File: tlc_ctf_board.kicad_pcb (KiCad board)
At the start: 2 copper layers, 78 x 51 mm, 15 parts, among them J1 AVR-ISP-6, U1 ATtiny84A-SSU

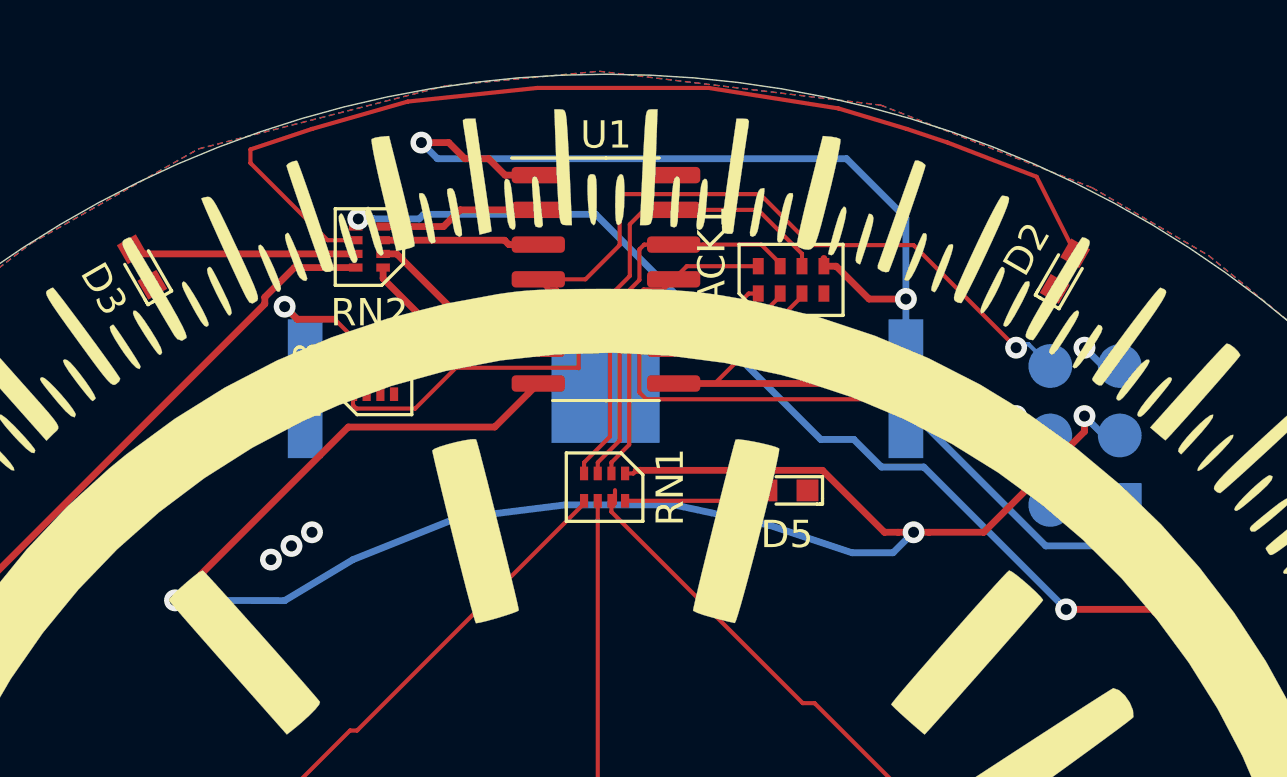
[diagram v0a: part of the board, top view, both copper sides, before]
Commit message: fix connections per qtouch, reroute.  switch to discrete caps
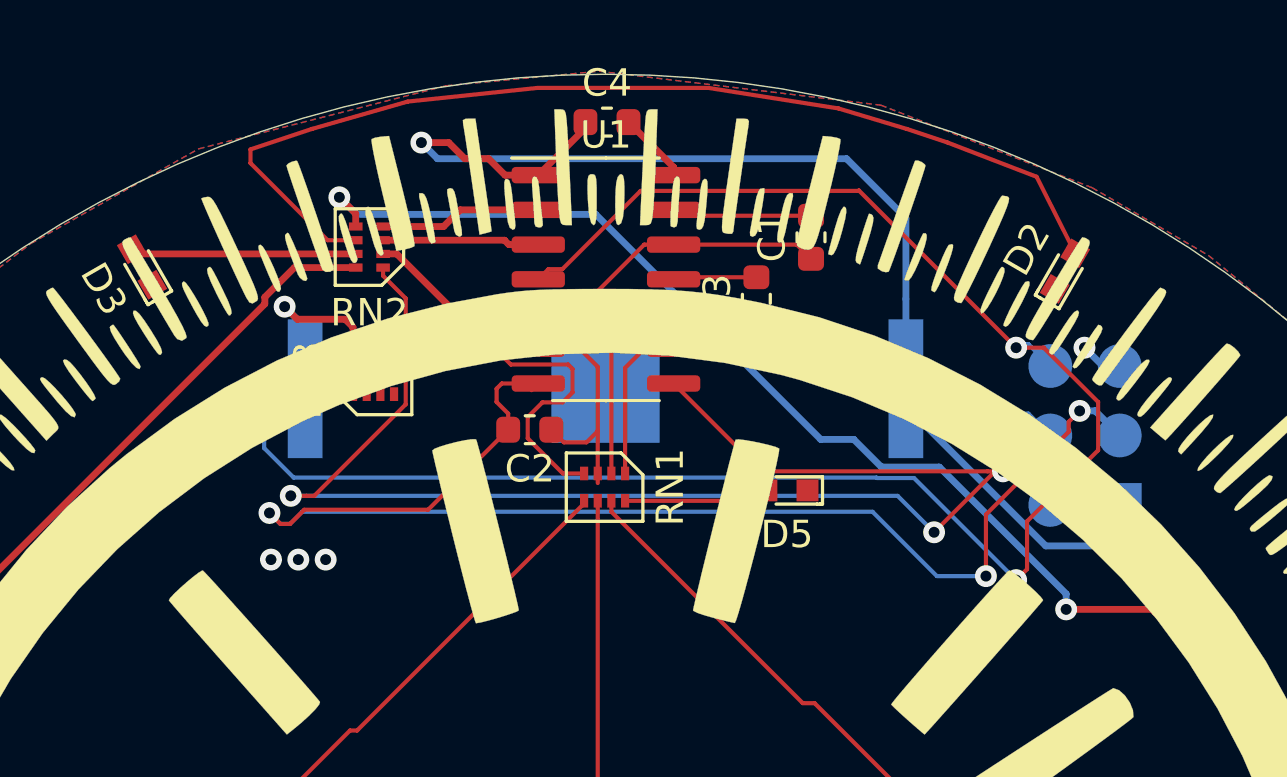
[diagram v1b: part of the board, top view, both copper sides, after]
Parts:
- removed CPACK1: C_Pack_4, tlc_ctf_board:CAP_ARRAY_4_1206
- removed the G*** at (174.0, 67.0) (x2)
- added C1: C, Capacitor_SMD:C_0603_1608Metric, F.Cu at (181.5, 47.4)
- added C2: C, Capacitor_SMD:C_0603_1608Metric, F.Cu at (171.2, 54.5)
- added C3: C, Capacitor_SMD:C_0603_1608Metric, F.Cu at (179.5, 49.7)
- added C4: C, Capacitor_SMD:C_0603_1608Metric, F.Cu at (174.0, 43.2)
- added G***: LOGO, tlc_ctf_board:logo, B.Cu at (174.0, 67.0)
- added G***: LOGO, tlc_ctf_board:logo, F.Cu at (174.0, 67.0)
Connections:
- J1 pad 1: MISO -> LED2
- J1 pad 3: QT5 -> LED1
- J1 pad 4: LED1 -> MOSI
- RN1 pad 2: QT2 -> SNSK1
- RN1 pad 3: QT3 -> SNSK2
- RN1 pad 4: QT1 -> SNSK0
- U1 pad 10: QT4 -> SNSK1
- U1 pad 11: QT2 -> SNS1
- U1 pad 12: QT3 -> SNSK0
- U1 pad 13: QT1 -> SNS0
- U1 pad 6: LED2 -> SNSK2
- U1 pad 7: LED1 -> MOSI
- U1 pad 8: MISO -> LED2
- U1 pad 9: QT5 -> LED1
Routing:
- net MOSI: track 0.00 -> 50.8 mm, vias 0 -> 3
- net LED2: track 7.14 -> 54.1 mm, vias 0 -> 3
- net LED1: track 66.5 -> 21.3 mm, vias 3 -> 1
- net RESET: track 37.6 -> 69.4 mm, vias 1 -> 3
- net QT5: track 25.7 -> 0.00 mm, vias 1 -> 0
- net SNSK0: track 0.00 -> 23.1 mm
- net MISO: track 22.4 -> 0.00 mm, vias 1 -> 0
- net QT1: track 17.4 -> 0.00 mm
- net QT3: track 14.4 -> 0.00 mm
- net QT2: track 11.8 -> 0.00 mm
- net SNSK1: track 0.00 -> 10.5 mm
- net SNSK2: track 0.00 -> 10.1 mm
- net SNS0: track 0.00 -> 5.11 mm
- net QT4: track 3.41 -> 0.00 mm
- net SNS1: track 0.00 -> 3.06 mm
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
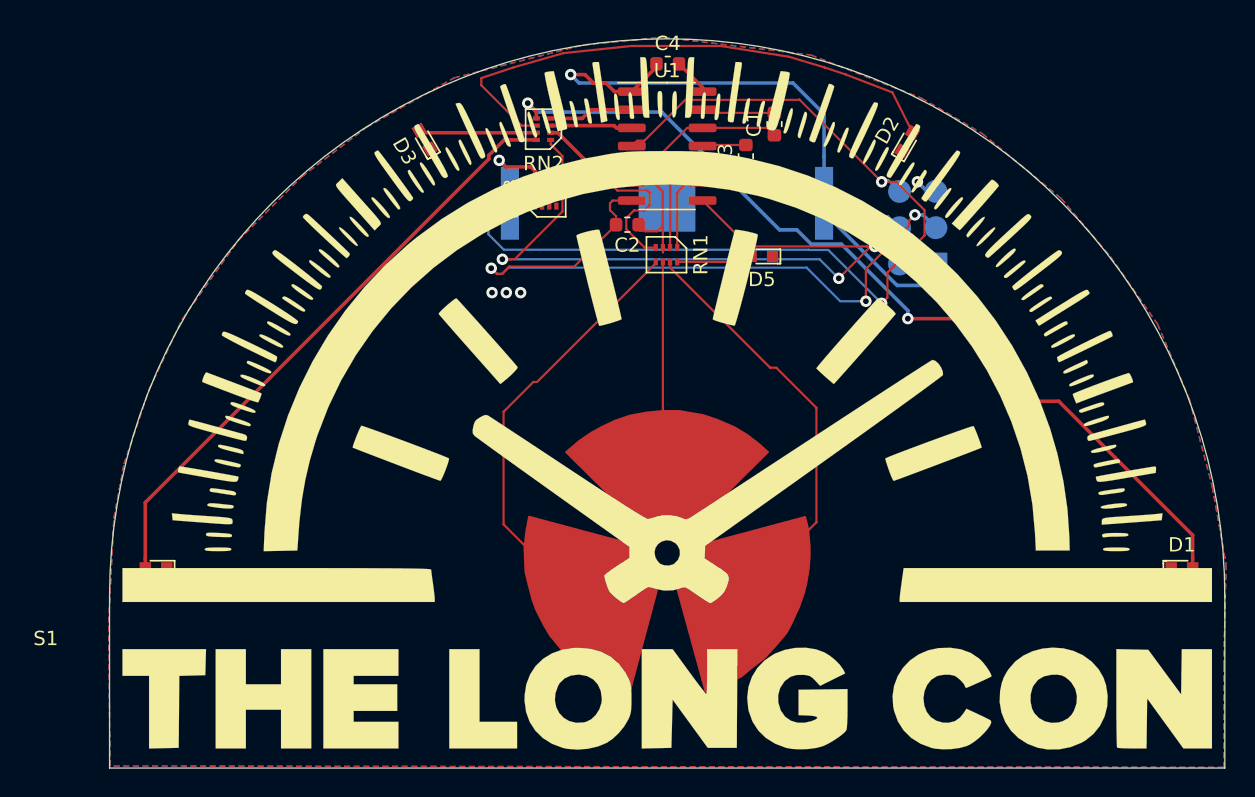
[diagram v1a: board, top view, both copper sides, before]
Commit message: adjust pads on battery, add oshw logo
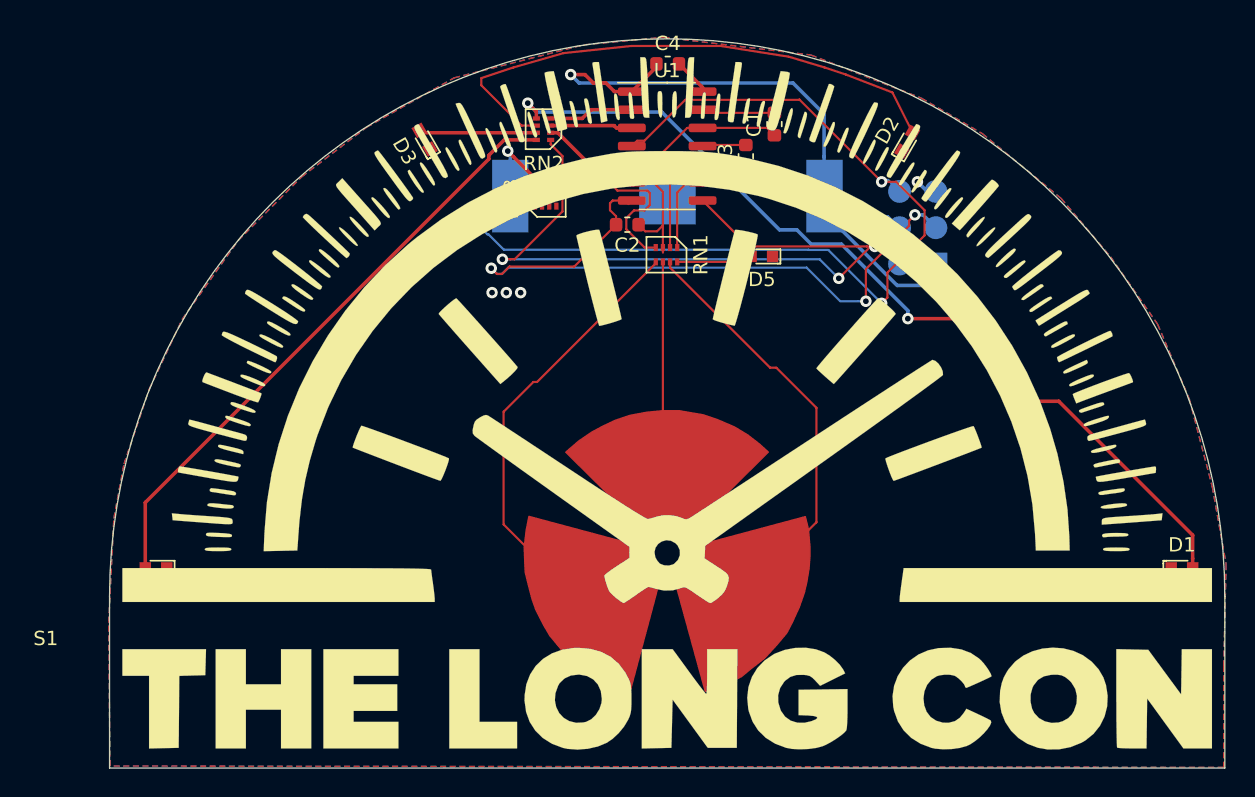
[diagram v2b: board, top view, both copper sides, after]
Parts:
- added REF**: OSHW-Logo2_9.8x8mm_SilkScreen, Symbol:OSHW-Logo2_9.8x8mm_SilkScreen, B.Cu at (173.7, 69.0)
- moved BT1 0.50 mm to (174.0, 52.5)
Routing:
- net VCC: track 53.6 -> 55.2 mm
- net RESET: track 69.4 -> 70.5 mm

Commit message: add last changes
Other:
- board text added: "v0.2"
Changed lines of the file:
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@@
   (general
     (thickness 1.6)
-    (drawings 8)
+    (drawings 9)
     (tracks 235)
     (zones 0)
@@
       (plotinvisibletext false)
       (padsonsilk false)
-      (subtractmaskfromsilk false)
+      (subtractmaskfromsilk true)
       (outputformat 1)
       (mirror false)
-      (drillshape 1)
+      (drillshape 0)
       (scaleselection 1)
-      (outputdirectory ""))
+      (outputdirectory "plots/v0.2/"))
   )
   (net 0 "")
@@
     (pad 6 smd oval (at 2.54 -5.08) (size 1.6 1.6) (layers B.Cu B.Paste B.Mask)
       (net 1 GND))
+    (model ${KISYS3DMOD}/Connector_PinHeader_2.54mm.3dshapes/PinHeader_2x03_P2.54mm_Vertical.step
+      (at (xyz 0 0 0))
+      (scale (xyz 1 1 1))
+      (rotate (xyz 0 0 0))
+    )
   )
   (module tlc_ctf_board:r_array (layer F.Cu)
@@
       (net 22 "Net-(RN3-Pad4)"))
   )
+  (gr_text v0.2 (at 173.74 73.72) (layer B.SilkS)
+    (effects (font (size 1 1) (thickness 0.15)) (justify mirror))
+  )
   (gr_circle (center 173.99 77.47) (end 193.99 77.47) (layer Eco1.User) (width 0.15))
